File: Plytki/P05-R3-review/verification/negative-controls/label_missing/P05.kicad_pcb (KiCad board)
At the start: 2 copper layers, 106.5 x 100 mm, 127 parts, among them J4 TAPS / PTH, J6 AUX / coax 50mm, K1 G6K-2P-Y DC5, K2 G6K-2P-Y DC5, K3 G6K-2P-Y DC5, SW1 AUX HI / LO, U1 AD7606BBSTZ, U10 74LVC125AD, U11 74LVC125AD, U12 MCP1700-3302E/TO, U2 REF5025IDR, U3 TLV1702-Q1, U4 TBD62083APG, U5 SN74HC08N, U6 MCP120-300DI/TO, U7 MCP120-450DI/TO, U8 74LVC125AD, U9 74LVC125AD

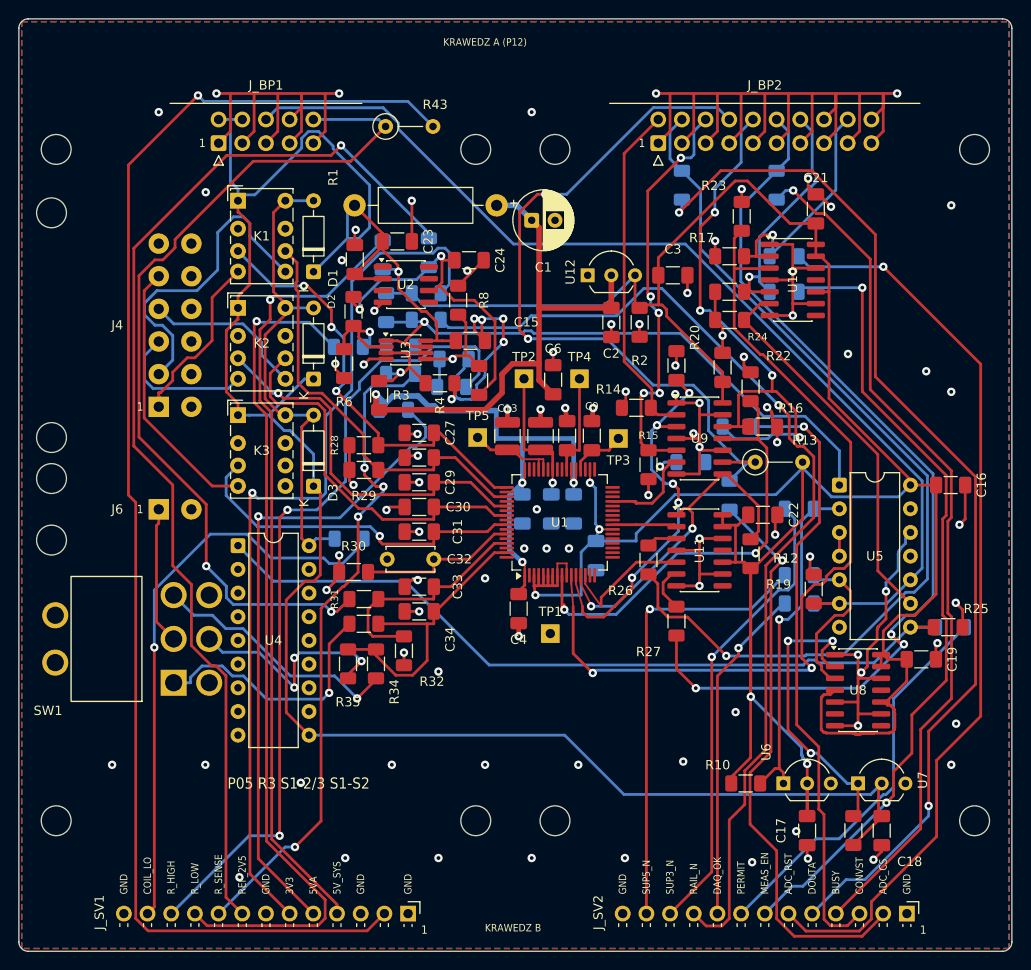
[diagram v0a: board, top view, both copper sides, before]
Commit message: P05 R3: poprawki po niezależnej recenzji PCB (2.10) — masa przy U1, drogi powrotne, nadruk 1,0/0,15 mm
- MAJOR-1: bez paska 5VA (y 45) i kręgosłupa pod pinami wejść; łączniki 5VA pionowo między kondensatorami,
  AVCC 1 kręgosłupem wewnątrz pierścienia; przelotki GND pod korpusami kondensatorów, przy AGND/REFGND,
  pod każdym 100 nF, kolumna przy pinach wejść; 12 przelotek wewnątrz pierścienia (było 4)
- MAJOR-2: strefy routera na B.Cu pod wachlarzem wejść i kondensatorami U1; kondensatory odsprzęgające
  według pinu zasilania i GND; przelotki GND przy kondensatorach; tory masy z planera (C15, C18)
- MINOR: reguła 0,15 mm dla wylewek tylko w pierścieniu pól (obszary DRC_ONLY_*), VBAT >= 0,6 mm od TAP,
  rzeczywiste długości SPI w README, nadruk 1,0/0,15 mm, tabliczka P05-R3
- nowe kontrole dróg powrotnych masy (src/gndpath.py); dziewięć pozycji przyjętych jawnie (decyzja 1
  użytkownika 2.10, limity = zmierzone + ok. 1 mm)
- DRC 0/0/0 (4 x lib_footprint_mismatch przyjęte), kontrole PCB 36/36, próby ujemne 35/35

Co-Authored-By: Claude Opus 5.5 <noreply@anthropic.com>
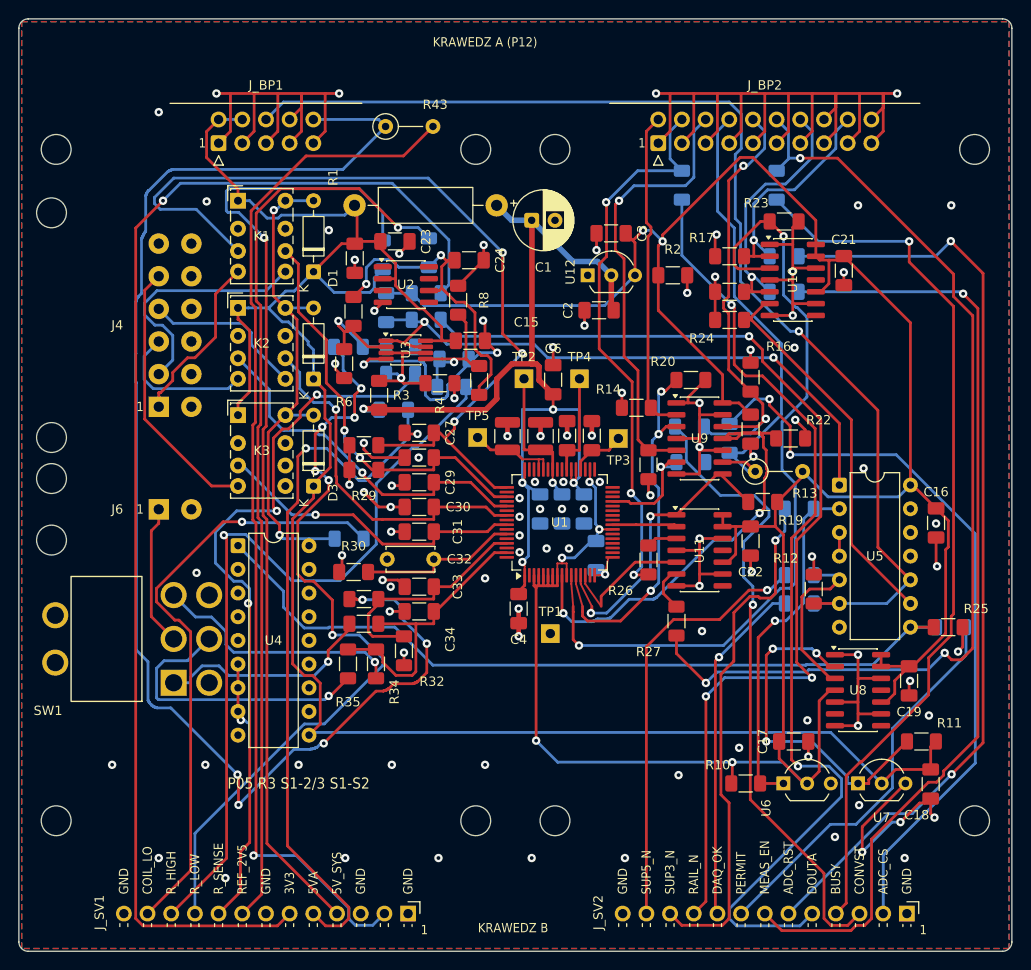
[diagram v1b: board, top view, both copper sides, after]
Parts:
- moved R11 12.0 mm to (96.8, 77.5), turned to 0 degrees
- moved C17 9.67 mm to (83.1, 77.5), turned to 0 degrees
- moved C3 8.01 mm to (63.5, 23.0), turned to 180 degrees
- moved C20 7.27 mm to (78.5, 44.0), turned to -90 degrees
- moved C21 7.27 mm to (88.5, 27.0), turned to -90 degrees
- moved C18 7.25 mm to (97.8, 82.1)
- moved R22 7.02 mm to (82.8, 45.0), turned to 0 degrees
- moved R2 6.17 mm to (70.1, 27.5), turned to 0 degrees
- moved R45 6.10 mm to (76.2, 45.0), turned to 90 degrees
- moved R19 5.70 mm to (79.8, 51.8), turned to 0 degrees
- moved R16 5.46 mm to (78.5, 38.4), turned to 90 degrees
- moved R46 5.10 mm to (71.9, 43.7), turned to 180 degrees
- moved R23 4.58 mm to (82.1, 21.7), turned to 0 degrees
- moved C16 4.35 mm to (98.4, 54.1), turned to -90 degrees
- moved C22 3.10 mm to (78.5, 56.0), turned to -90 degrees
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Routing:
- net VBAT_SENSE: track 94.4 -> 148.7 mm, vias 2 -> 5
- net ADC_CH1: track 47.5 -> 94.9 mm
- net /SERWIS/SRV_3V3_DAQ: track 96.1 -> 135.6 mm
- net ADC_DOUTA: track 99.7 -> 60.3 mm, vias 1 -> 3
- net /SERWIS/SRV_VBAT_SENSE: track 146.2 -> 111.3 mm
- net ADC_CS: track 80.0 -> 49.7 mm, vias 2 -> 0
- net /SERWIS/SRV_5V_SYS: track 84.4 -> 104.3 mm
- net /SERWIS/SRV_REF_2V5: track 117.1 -> 98.3 mm
- net /SERWIS/SRV_ADC_CS: track 62.3 -> 80.5 mm, vias 1 -> 2
- net /SERWIS/SRV_MEAS_EN: track 86.9 -> 103.4 mm, vias 2 -> 1
- net GND: track 350.6 -> 363.1 mm, vias 96 -> 104
- net DAQ_OK: track 113.1 -> 125.0 mm, vias 0 -> 1
- net ADC_CONVST: track 60.8 -> 49.2 mm, vias 4 -> 2
- net 5V_SYS: track 226.6 -> 215.9 mm, vias 1 -> 0
- net 3V3_DAQ: track 317.0 -> 306.5 mm, vias 5 -> 7
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
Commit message: P05 R3: nóżki SW1 na GND, C35 10 µF na AVCC przy U1 (decyzje użytkownika 2.10)
- footprint ESW_100DP_M6: nóżki mocujące jako pola pinu 4 (GND) — oprawa przełącznika na masie (ESD)
- schemat: C35 10 µF 1206 X7R na 5VA_P05 nad C6 (uwaga recenzji o pojemności AVCC przy U1)
- trasowanie zatwierdzonej wersji odtworzone (C35 w miejscu wolnym od miedzi); planer z szerokością PWR 0,6 mm
- kontrole PCB 36/36, próby ujemne 35/35

Co-Authored-By: Claude Opus 5.5 <noreply@anthropic.com>
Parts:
- added C35: 10u, Capacitor_SMD:C_1206_3216Metric_Pad1.33x1.80mm_HandSolder, F.Cu at (57.3, 35.0)
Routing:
- net GND: track 363.1 -> 360.8 mm, vias 104 -> 103
